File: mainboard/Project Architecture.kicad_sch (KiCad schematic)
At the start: 0 parts

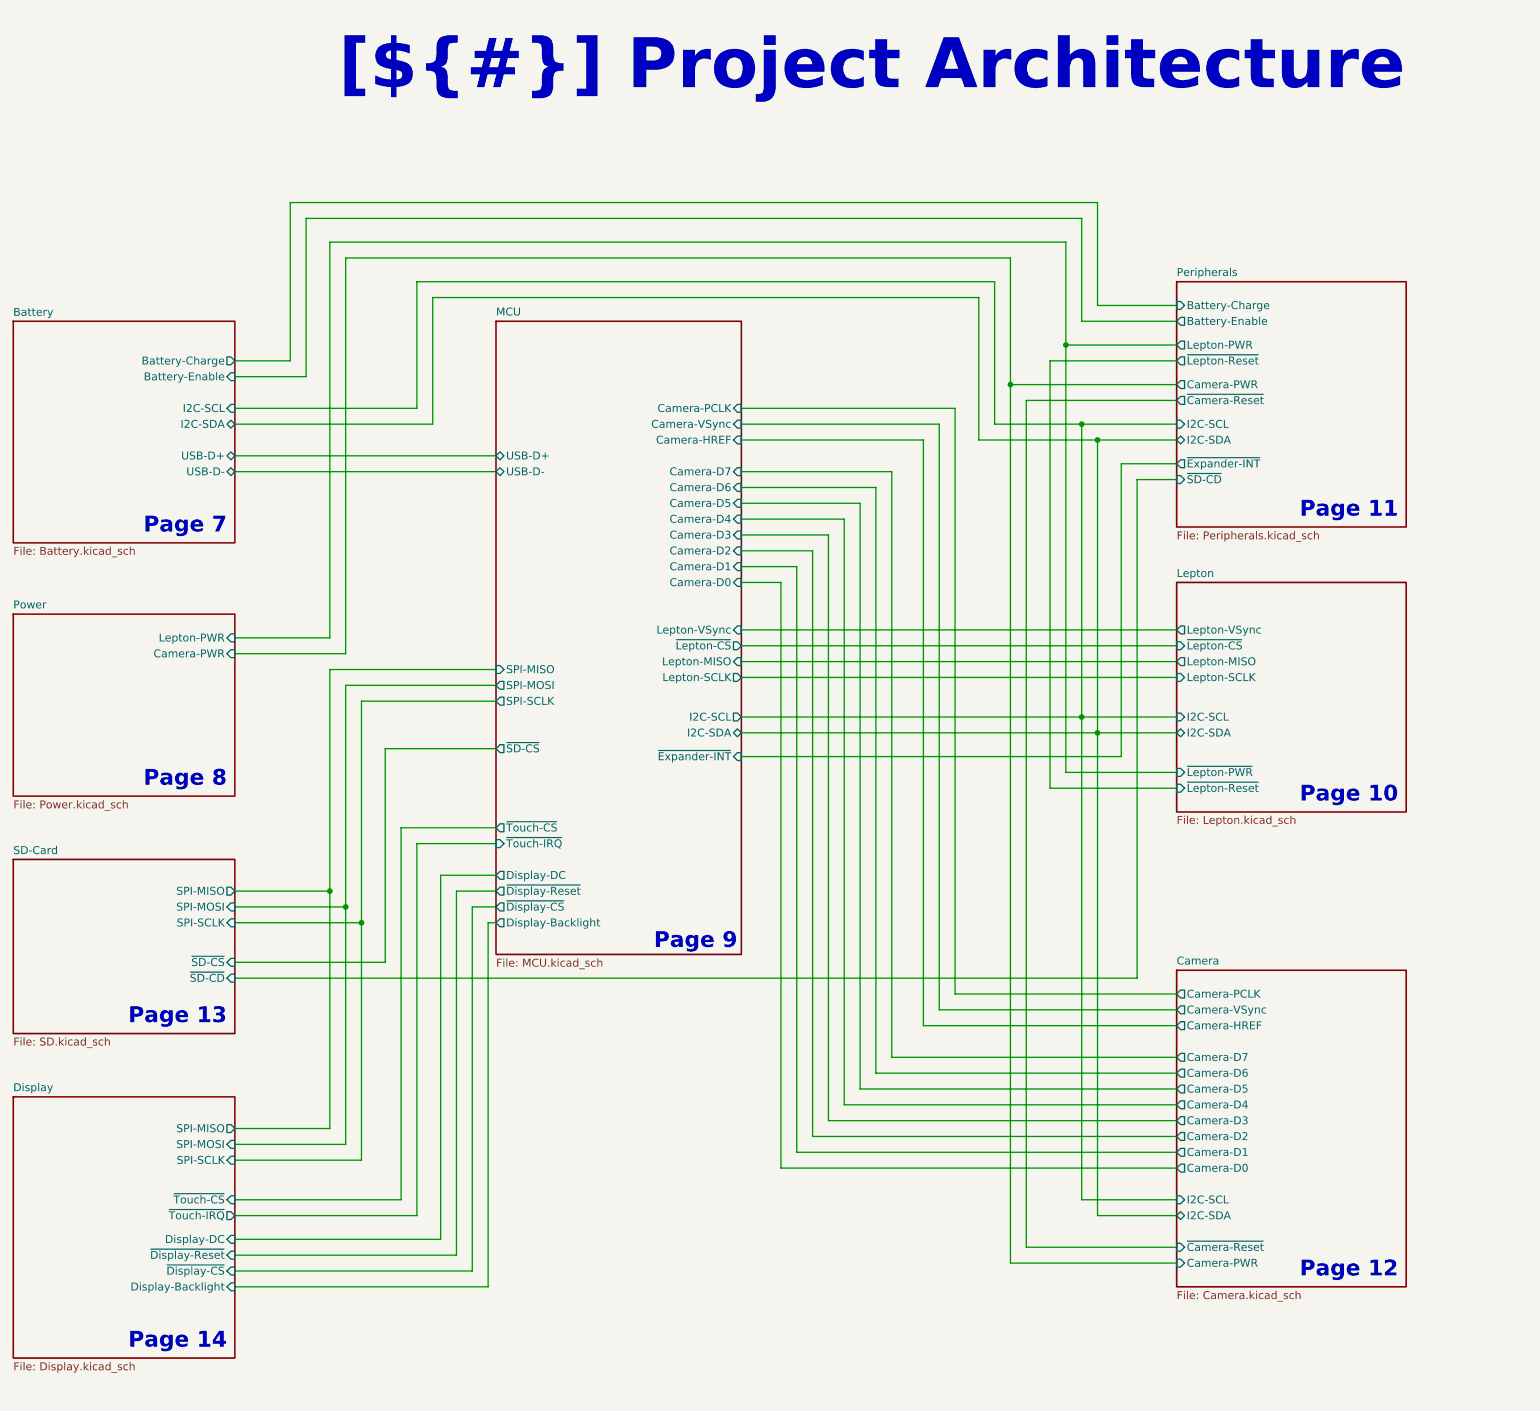
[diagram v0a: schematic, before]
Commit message: Continue routing, add flash LEDs for the RGB camera, add PWM controller for the Display Backlight and the flash LEDs, add Polyfuse for the battery
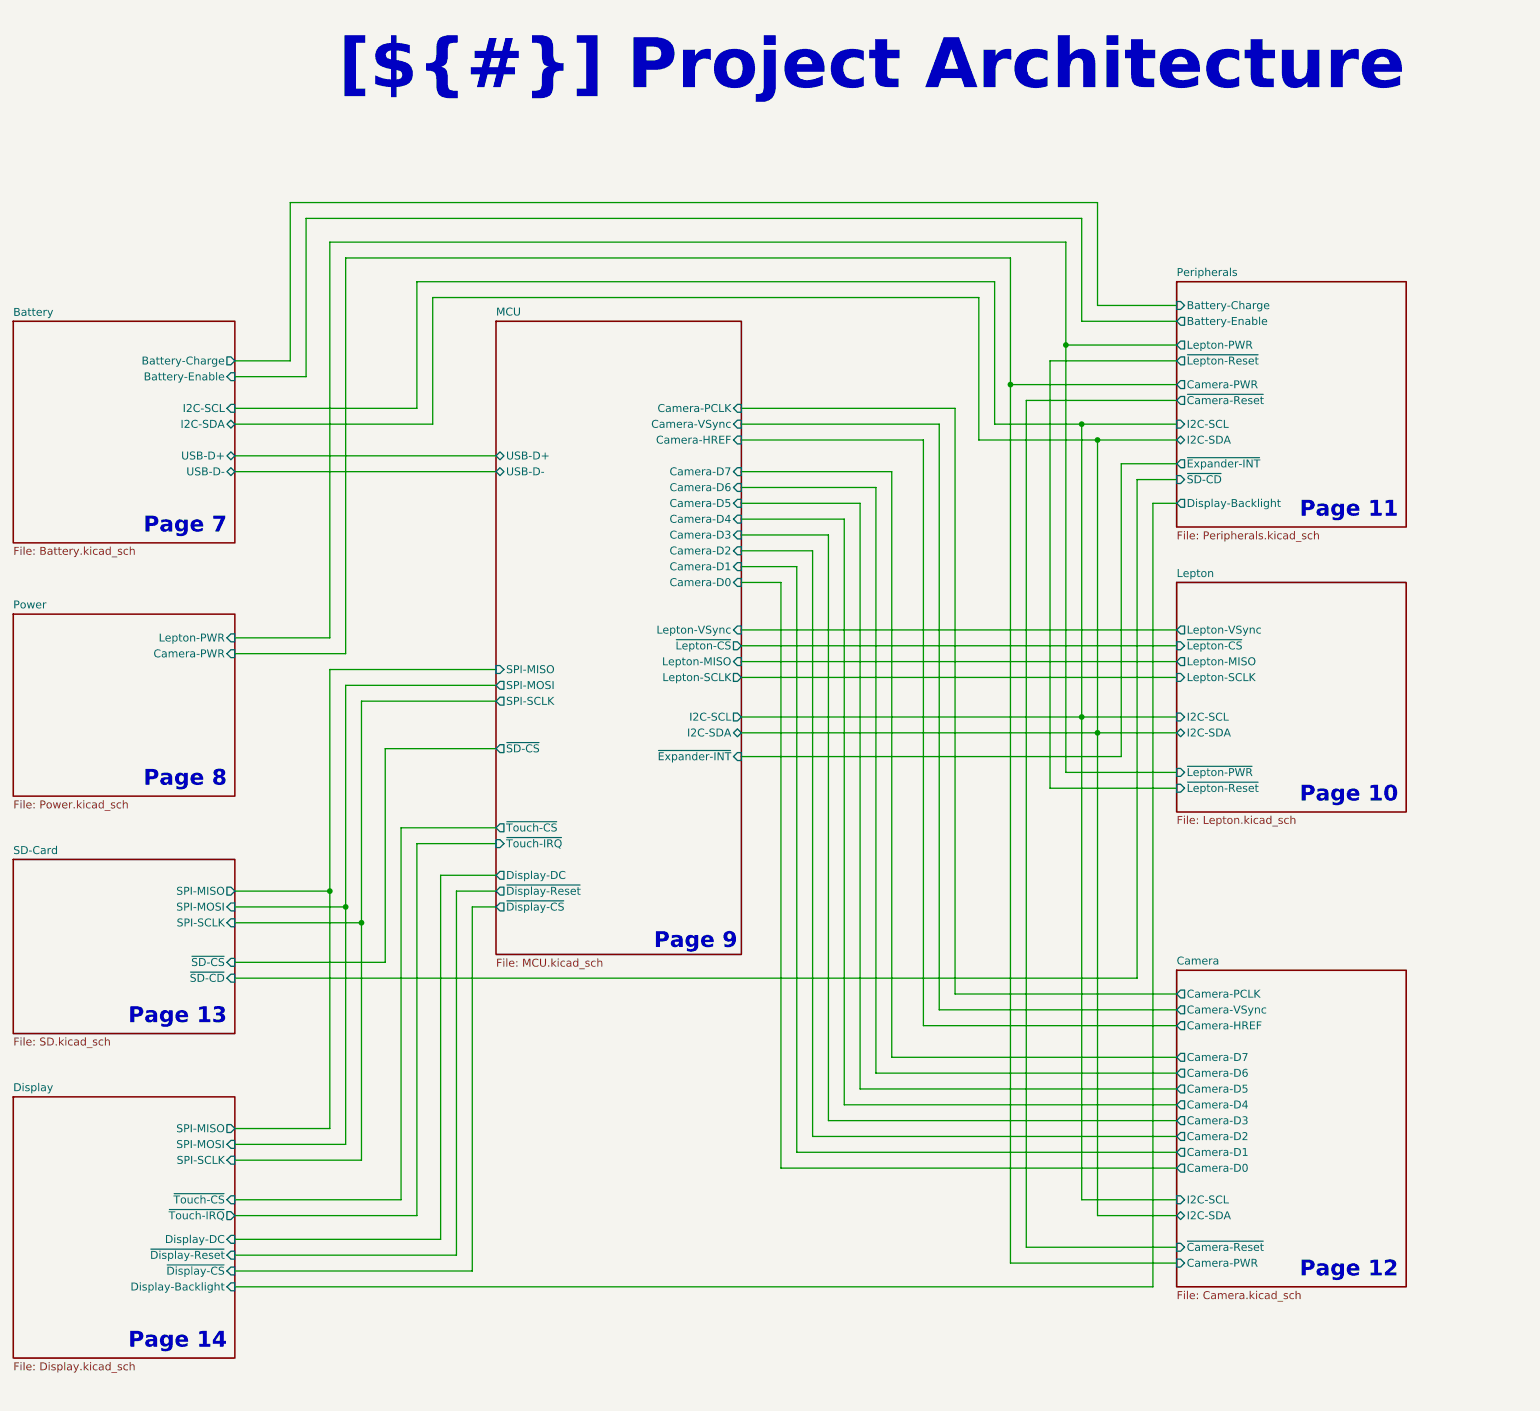
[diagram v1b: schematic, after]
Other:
- sheet MCU ports: added none; removed Display-Backlight
- sheet Peripherals ports: added Display-Backlight; removed none
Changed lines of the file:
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@@
-	(wire
-		(pts
-			(xy 107.95 215.9) (xy 148.59 215.9)
-		)
-		(stroke
-			(width 0)
-			(type default)
-		)
-	)
 	(wire
 		(pts
@@
 	(wire
 		(pts
+			(xy 259.08 90.17) (xy 255.27 90.17)
+		)
+		(stroke
+			(width 0)
+			(type default)
+		)
+	)
+	(wire
+		(pts
 			(xy 123.19 190.5) (xy 123.19 152.4)
 		)
@@
 	(wire
 		(pts
-			(xy 148.59 157.48) (xy 148.59 215.9)
-		)
-		(stroke
-			(width 0)
-			(type default)
-		)
-	)
-	(wire
-		(pts
 			(xy 259.08 64.77) (xy 241.3 64.77)
 		)
@@
 	(wire
 		(pts
-			(xy 149.86 157.48) (xy 148.59 157.48)
-		)
-		(stroke
-			(width 0)
-			(type default)
-		)
-	)
-	(wire
-		(pts
 			(xy 107.95 204.47) (xy 137.16 204.47)
 		)
@@
 	(wire
 		(pts
+			(xy 255.27 90.17) (xy 255.27 215.9)
+		)
+		(stroke
+			(width 0)
+			(type default)
+		)
+	)
+	(wire
+		(pts
 			(xy 140.97 149.86) (xy 149.86 149.86)
 		)
@@
 		(pts
 			(xy 107.95 85.09) (xy 149.86 85.09)
+		)
+		(stroke
+			(width 0)
+			(type default)
+		)
+	)
+	(wire
+		(pts
+			(xy 107.95 215.9) (xy 255.27 215.9)
 		)
 		(stroke
@@
 			)
 		)
-		(pin "Display-Backlight" output
-			(at 149.86 157.48 180)
-			(effects
-				(font
-					(size 1.27 1.27)
-				)
-				(justify left)
-			)
-		)
 		(instances
 			(project "Mainboard"
@@
 			(effects
 				(font
+					(size 1.27 1.27)
+				)
+				(justify left)
+			)
+		)
+		(pin "Display-Backlight" output
+			(at 259.08 90.17 180)
+			(effects
+				(font

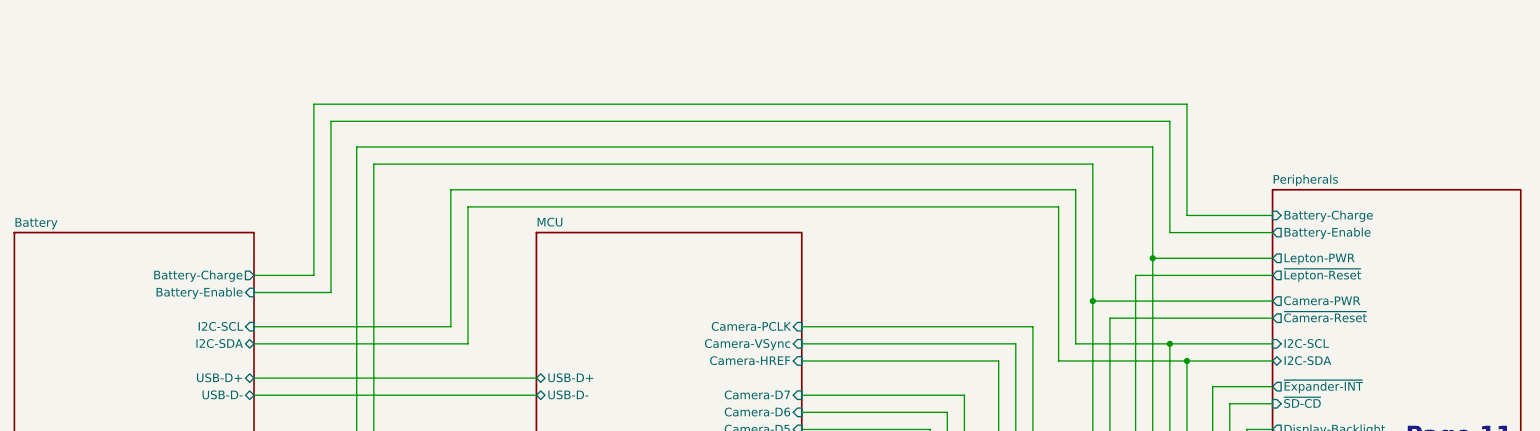
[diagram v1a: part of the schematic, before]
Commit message: Remove ADC for battery measurement and add a fuel gauge
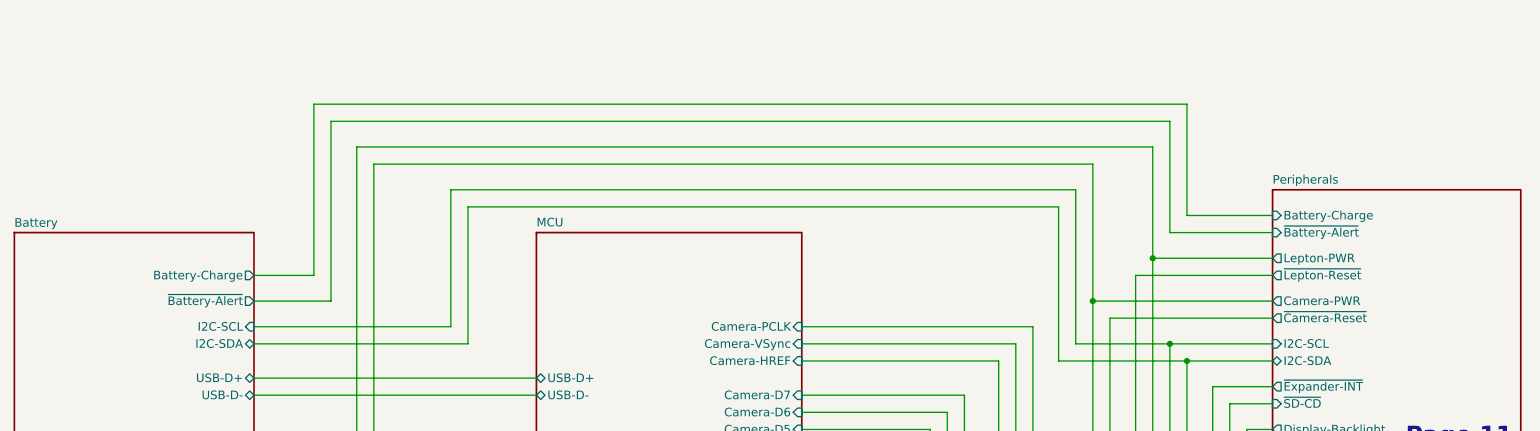
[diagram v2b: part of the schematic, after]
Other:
- sheet Battery ports: added ~{Battery-Alert}; removed Battery-Enable
- sheet Peripherals ports: added ~{Battery-Alert}; removed Battery-Enable

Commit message: Layout complete
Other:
- sheet Display ports: added I2C-SCL, I2C-SDA, ~{Display-Expander-Int}, ~{Touch-Reset}; removed ~{Touch-CS}
- sheet MCU ports: added ~{Display-Expander-Int}, ~{Expander-Int}, ~{Touch-Reset}; removed ~{Expander-INT}, ~{Touch-CS}
- sheet Peripherals ports: added ~{Expander-Int}; removed ~{Expander-INT}
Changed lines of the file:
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@@
 	(text "Page 14"
 		(exclude_from_sim no)
-		(at 106.68 226.06 0)
+		(at 106.934 230.124 0)
 		(effects
 			(font
@@
 	)
 	(junction
+		(at 246.38 204.47)
+		(diameter 0)
+		(color 0 0 0 0)
+	)
+	(junction
 		(at 128.27 157.48)
+		(diameter 0)
+		(color 0 0 0 0)
+	)
+	(junction
+		(at 243.84 201.93)
 		(diameter 0)
 		(color 0 0 0 0)
@@
 	(wire
 		(pts
-			(xy 125.73 193.04) (xy 125.73 154.94)
+			(xy 125.73 191.77) (xy 125.73 154.94)
 		)
 		(stroke
@@
 	(wire
 		(pts
-			(xy 143.51 152.4) (xy 149.86 152.4)
+			(xy 144.78 152.4) (xy 149.86 152.4)
 		)
 		(stroke
@@
 	(wire
 		(pts
-			(xy 128.27 195.58) (xy 128.27 157.48)
+			(xy 128.27 194.31) (xy 128.27 157.48)
+		)
+		(stroke
+			(width 0)
+			(type default)
+		)
+	)
+	(wire
+		(pts
+			(xy 193.04 219.71) (xy 193.04 201.93)
 		)
 		(stroke
@@
 	(wire
 		(pts
-			(xy 107.95 195.58) (xy 128.27 195.58)
+			(xy 107.95 219.71) (xy 193.04 219.71)
+		)
+		(stroke
+			(width 0)
+			(type default)
+		)
+	)
+	(wire
+		(pts
+			(xy 107.95 194.31) (xy 128.27 194.31)
+		)
+		(stroke
+			(width 0)
+			(type default)
+		)
+	)
+	(wire
+		(pts
+			(xy 133.35 198.12) (xy 133.35 138.43)
 		)
 		(stroke
@@
 	(wire
 		(pts
-			(xy 143.51 210.82) (xy 143.51 152.4)
-		)
-		(stroke
-			(width 0)
-			(type default)
-		)
-	)
-	(wire
-		(pts
-			(xy 107.95 193.04) (xy 125.73 193.04)
+			(xy 144.78 210.82) (xy 144.78 152.4)
+		)
+		(stroke
+			(width 0)
+			(type default)
+		)
+	)
+	(wire
+		(pts
+			(xy 107.95 191.77) (xy 125.73 191.77)
 		)
 		(stroke
@@
 	(wire
 		(pts
-			(xy 132.08 129.54) (xy 149.86 129.54)
+			(xy 130.81 129.54) (xy 149.86 129.54)
 		)
 		(stroke
@@
 	(wire
 		(pts
-			(xy 107.95 163.83) (xy 132.08 163.83)
+			(xy 107.95 163.83) (xy 130.81 163.83)
 		)
 		(stroke
@@
 	(wire
 		(pts
+			(xy 193.04 201.93) (xy 243.84 201.93)
+		)
+		(stroke
+			(width 0)
+			(type default)
+		)
+	)
+	(wire
+		(pts
 			(xy 234.95 209.55) (xy 259.08 209.55)
 		)
@@
 	(wire
 		(pts
-			(xy 134.62 201.93) (xy 107.95 201.93)
+			(xy 135.89 201.93) (xy 107.95 201.93)
 		)
 		(stroke
@@
 	(wire
 		(pts
-			(xy 137.16 204.47) (xy 137.16 144.78)
+			(xy 138.43 204.47) (xy 138.43 144.78)
+		)
+		(stroke
+			(width 0)
+			(type default)
+		)
+	)
+	(wire
+		(pts
+			(xy 107.95 198.12) (xy 133.35 198.12)
 		)
 		(stroke
@@
 	(wire
 		(pts
-			(xy 123.19 190.5) (xy 123.19 152.4)
+			(xy 123.19 189.23) (xy 123.19 152.4)
 		)
 		(stroke
@@
 	(wire
 		(pts
-			(xy 107.95 210.82) (xy 143.51 210.82)
+			(xy 107.95 210.82) (xy 144.78 210.82)
 		)
 		(stroke
@@
 	(wire
 		(pts
-			(xy 134.62 142.24) (xy 134.62 201.93)
+			(xy 135.89 142.24) (xy 135.89 201.93)
 		)
 		(stroke
@@
 	(wire
 		(pts
-			(xy 146.05 154.94) (xy 149.86 154.94)
+			(xy 147.32 154.94) (xy 149.86 154.94)
 		)
 		(stroke
@@
 	(wire
 		(pts
-			(xy 107.95 204.47) (xy 137.16 204.47)
-		)
-		(stroke
-			(width 0)
-			(type default)
-		)
-	)
-	(wire
-		(pts
-			(xy 140.97 208.28) (xy 107.95 208.28)
+			(xy 107.95 204.47) (xy 138.43 204.47)
+		)
+		(stroke
+			(width 0)
+			(type default)
+		)
+	)
+	(wire
+		(pts
+			(xy 142.24 208.28) (xy 107.95 208.28)
 		)
 		(stroke
@@
 	(wire
 		(pts
-			(xy 140.97 149.86) (xy 149.86 149.86)
+			(xy 142.24 149.86) (xy 149.86 149.86)
 		)
 		(stroke
@@
 	(wire
 		(pts
+			(xy 133.35 138.43) (xy 149.86 138.43)
+		)
+		(stroke
+			(width 0)
+			(type default)
+		)
+	)
+	(wire
+		(pts
 			(xy 246.38 80.01) (xy 227.33 80.01)
 		)
@@
 	(wire
 		(pts
-			(xy 140.97 149.86) (xy 140.97 208.28)
+			(xy 142.24 149.86) (xy 142.24 208.28)
 		)
 		(stroke
@@
 	(wire
 		(pts
-			(xy 107.95 190.5) (xy 123.19 190.5)
+			(xy 107.95 189.23) (xy 123.19 189.23)
 		)
 		(stroke
@@
 	(wire
 		(pts
+			(xy 195.58 222.25) (xy 107.95 222.25)
+		)
+		(stroke
+			(width 0)
+			(type default)
+		)
+	)
+	(wire
+		(pts
 			(xy 210.82 87.63) (xy 189.23 87.63)
 		)
@@
 	(wire
 		(pts
-			(xy 149.86 142.24) (xy 134.62 142.24)
+			(xy 149.86 142.24) (xy 135.89 142.24)
 		)
 		(stroke
@@
 	(wire
 		(pts
+			(xy 246.38 204.47) (xy 195.58 204.47)
+		)
+		(stroke
+			(width 0)
+			(type default)
+		)
+	)
+	(wire
+		(pts
 			(xy 119.38 44.45) (xy 243.84 44.45)
 		)
@@
 	(wire
 		(pts
-			(xy 132.08 129.54) (xy 132.08 163.83)
+			(xy 195.58 204.47) (xy 195.58 222.25)
+		)
+		(stroke
+			(width 0)
+			(type default)
+		)
+	)
+	(wire
+		(pts
+			(xy 130.81 129.54) (xy 130.81 163.83)
 		)
 		(stroke
@@
 	(wire
 		(pts
-			(xy 146.05 213.36) (xy 146.05 154.94)
+			(xy 147.32 213.36) (xy 147.32 154.94)
 		)
 		(stroke
@@
 	(wire
 		(pts
-			(xy 107.95 213.36) (xy 146.05 213.36)
+			(xy 107.95 213.36) (xy 147.32 213.36)
 		)
 		(stroke
@@
 	(wire
 		(pts
-			(xy 137.16 144.78) (xy 149.86 144.78)
+			(xy 138.43 144.78) (xy 149.86 144.78)
 		)
 		(stroke
@@
 			)
 		)
-		(pin "~{Expander-INT}" input
+		(pin "~{Expander-Int}" input
 			(at 189.23 130.81 0)
 			(effects
@@
 			)
 		)
-		(pin "~{Touch-CS}" output
+		(pin "~{Touch-Reset}" output
 			(at 149.86 142.24 180)
 			(effects
@@
 				)
 				(justify right)
+			)
+		)
+		(pin "~{Display-Expander-Int}" input
+			(at 149.86 138.43 180)
+			(effects
+				(font
+					(size 1.27 1.27)
+				)
+				(justify left)
 			)
 		)
@@
 	(sheet
 		(at 72.39 185.42)
-		(size 35.56 41.91)
+		(size 35.56 45.72)
 		(exclude_from_sim no)
 		(in_bom yes)
@@
 		)
 		(property "Sheetfile" "Display.kicad_sch"
-			(at 72.39 227.9654 0)
+			(at 72.39 231.7754 0)
 			(effects
 				(font
@@
 		)
 		(pin "SPI-SCLK" input
-			(at 107.95 195.58 0)
+			(at 107.95 194.31 0)
 			(effects
 				(font
@@
 		)
 		(pin "SPI-MOSI" input
-			(at 107.95 193.04 0)
+			(at 107.95 191.77 0)
 			(effects
 				(font
@@
 		)
 		(pin "SPI-MISO" output
-			(at 107.95 190.5 0)
-			(effects
-				(font
-					(size 1.27 1.27)
-				)
-				(justify right)
-			)
-		)
-		(pin "~{Touch-CS}" input
+			(at 107.95 189.23 0)
+			(effects
+				(font
+					(size 1.27 1.27)
+				)
+				(justify right)
+			)
+		)
+		(pin "~{Touch-Reset}" input
 			(at 107.95 201.93 0)
 			(effects
@@
 		(pin "Display-Backlight" input
 			(at 107.95 215.9 0)
+			(effects
+				(font
+					(size 1.27 1.27)
+				)
+				(justify right)
+			)
+		)
+		(pin "I2C-SCL" input
+			(at 107.95 219.71 0)
+			(effects
+				(font
+					(size 1.27 1.27)
+				)
+				(justify right)
+			)
+		)
+		(pin "I2C-SDA" bidirectional
+			(at 107.95 222.25 0)
+			(effects
+				(font
+					(size 1.27 1.27)
+				)
+				(justify right)
+			)
+		)
+		(pin "~{Display-Expander-Int}" output
+			(at 107.95 198.12 0)
 			(effects
 				(font
@@
 			)
 		)
-		(pin "~{Expander-INT}" output
+		(pin "~{Expander-Int}" output
 			(at 259.08 83.82 180)
 			(effects
